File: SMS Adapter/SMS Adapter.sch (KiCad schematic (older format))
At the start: 3 parts, among them J1 c64_idc, J2 sms_joypad, J3 FIRE_SWAP

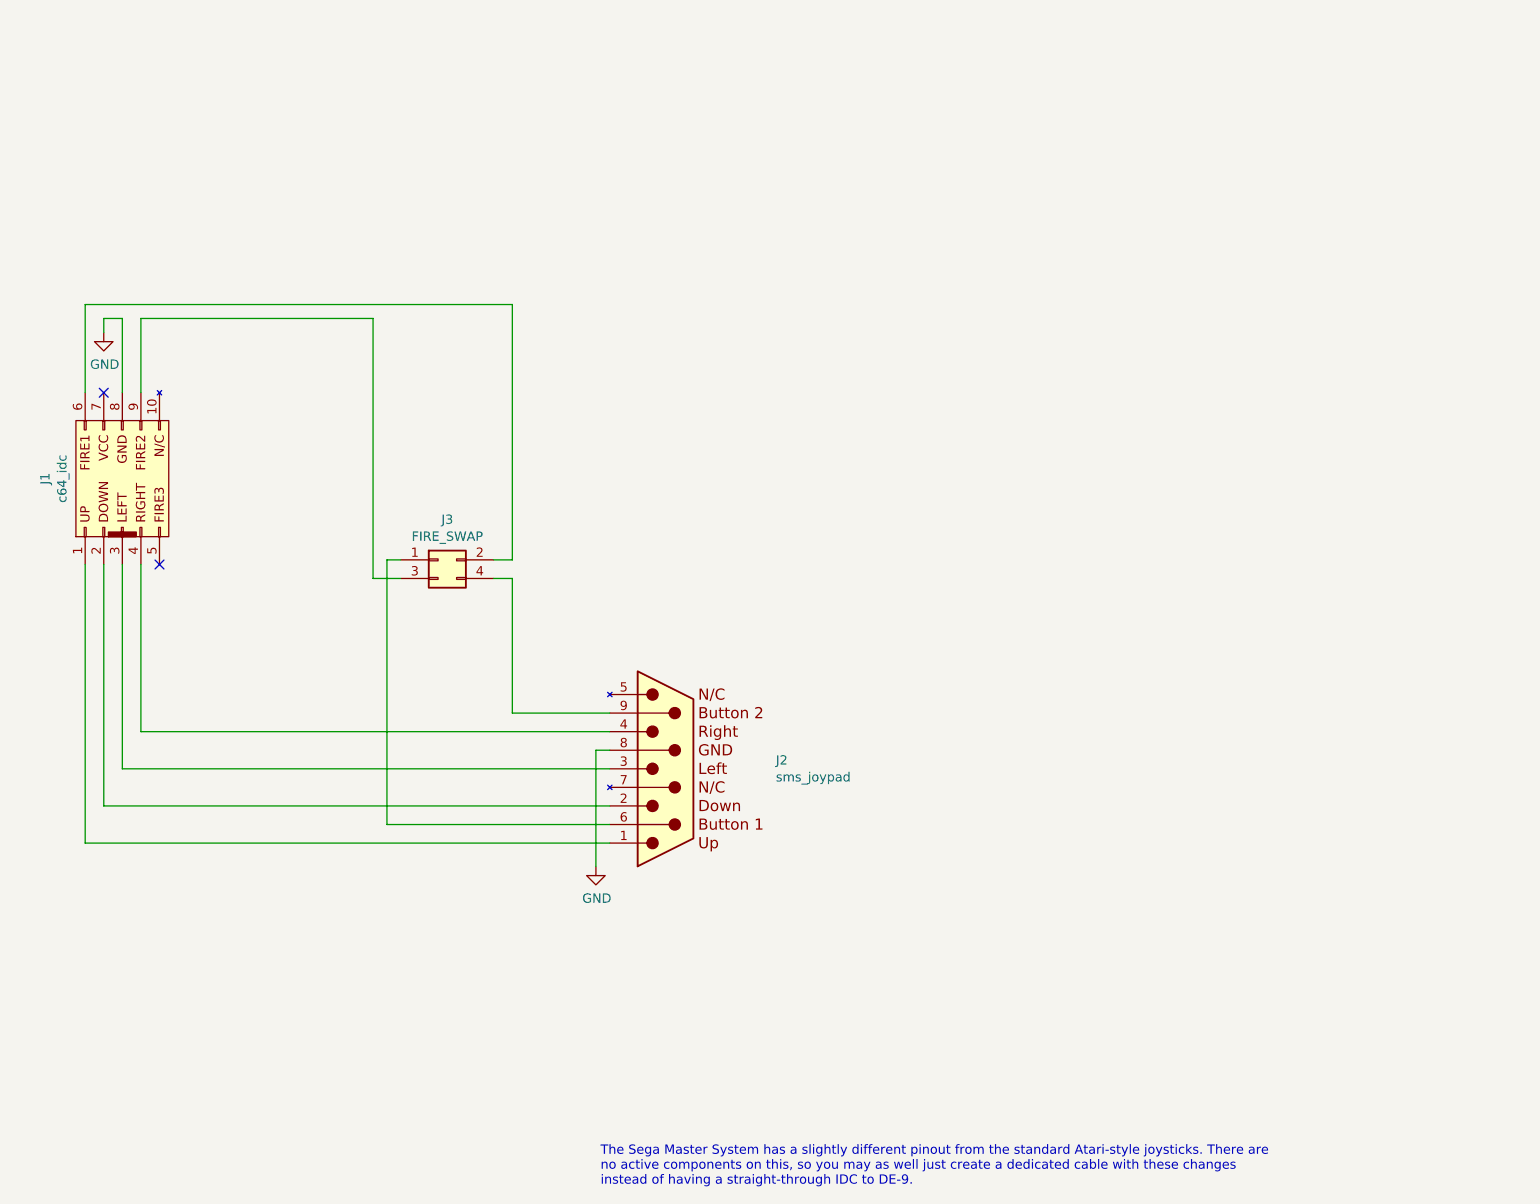
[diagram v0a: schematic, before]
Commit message: Added SMS jumper settings to schematic
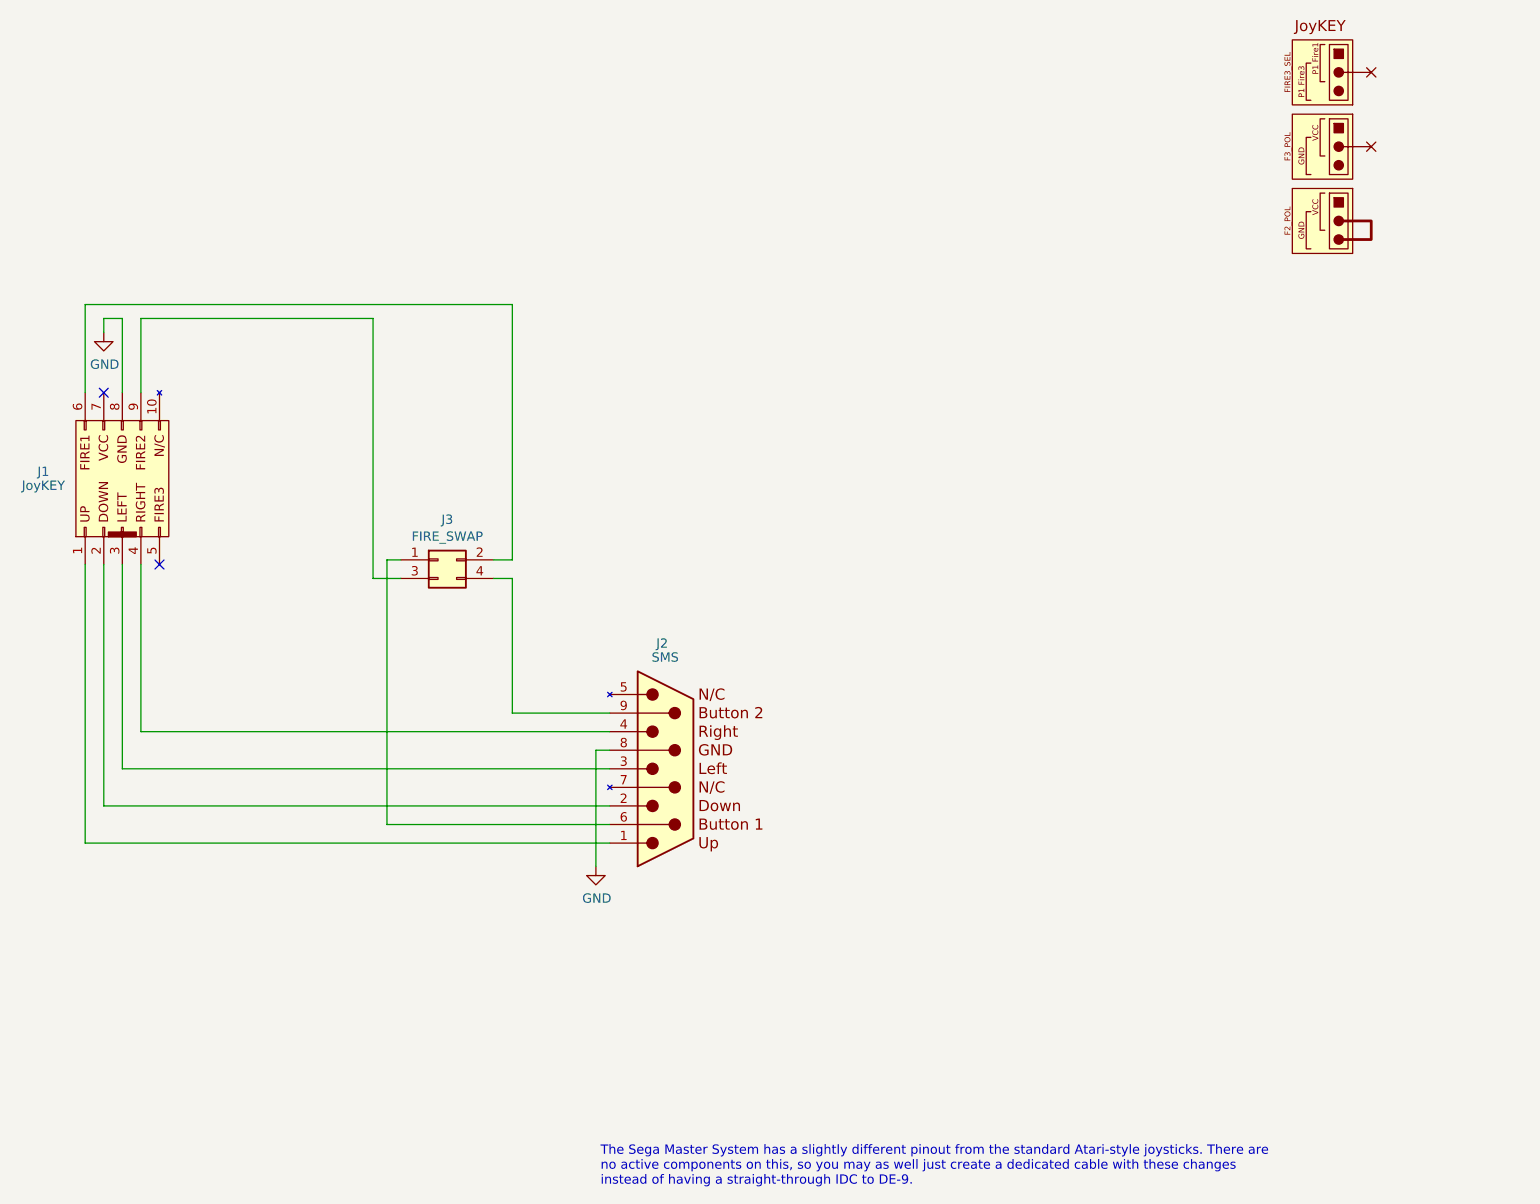
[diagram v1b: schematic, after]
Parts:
- J1: value c64_idc -> JoyKEY
- J2: value sms_joypad -> SMS
- J3: footprint (none) -> Pin_Headers:Pin_Header_Straight_2x02_Pitch2.54mm
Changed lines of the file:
@@
 U 1 1 5FD1F19D
 P 4425 3000
-F 0 "J1" H 4437 3415 50  0000 C CNN
-F 1 "c64_idc" H 4437 3324 50  0000 C CNN
+F 0 "J1" V 4475 3425 50  0000 C CNN
+F 1 "JoyKEY" V 4400 3425 50  0000 C CNN
 F 2 "" H 4425 3000 50  0001 C CNN
 F 3 "~" H 4425 3000 50  0001 C CNN
@@
 U 1 1 5FD232F5
 P 7350 4550
-F 0 "J2" H 7944 4596 50  0000 L CNN
-F 1 "sms_joypad" H 7944 4505 50  0000 L CNN
+F 0 "J2" H 7300 5225 50  0000 L CNN
+F 1 "SMS" H 7275 5150 50  0000 L CNN
 F 2 "" H 7350 4550 50  0001 C CNN
 F 3 "" H 7350 4550 50  0001 C CNN
@@
 F 0 "J3" H 6175 3642 50  0000 C CNN
 F 1 "FIRE_SWAP" H 6175 3551 50  0000 C CNN
-F 2 "" H 6125 3425 50  0001 C CNN
+F 2 "Pin_Headers:Pin_Header_Straight_2x02_Pitch2.54mm" H 6125 3425 50  0001 C CNN
 F 3 "~" H 6125 3425 50  0001 C CNN
 	1    6125 3425
@@
 Text Notes 7000 6800 0    50   ~ 0
 The Sega Master System has a slightly different pinout from the standard Atari-style joysticks. There are\nno active components on this, so you may as well just create a dedicated cable with these changes \ninstead of having a straight-through IDC to DE-9.
+$Comp
+L joykey_jumpers:JUMPER_SETTINGS_1 #1
+U 1 1 5FD24880
+P 10975 700
+F 0 "#1" H 10875 825 50  0001 C CNN
+F 1 "JUMPER_SETTINGS_1" H 10850 -450 50  0001 C CNN
+F 2 "" H 10975 525 50  0001 C CNN
+F 3 "~" H 10975 525 50  0001 C CNN
+	1    10975 700
+	1    0    0    -1
+$EndComp
+$Comp
+L joykey_jumpers:JUMPER_CONNECTED #4
+U 1 1 5FD250F4
+P 10975 1650
+F 0 "#4" H 10975 1550 50  0001 C CNN
+F 1 "JUMPER_CONNECTED" H 10975 1750 50  0001 C CNN
+F 2 "" H 10975 1650 50  0001 C CNN
+F 3 "" H 10975 1650 50  0001 C CNN
+	1    10975 1650
+	1    0    0    -1
+$EndComp
+$Comp
+L joykey_jumpers:JUMPER_NOT_CONNECTED #3
+U 1 1 5FD25605
+P 10975 1200
+F 0 "#3" H 10975 1125 50  0001 C CNN
+F 1 "JUMPER_NOT_CONNECTED" H 10975 1300 50  0001 C CNN
+F 2 "" H 10975 1200 50  0001 C CNN
+F 3 "" H 10975 1200 50  0001 C CNN
+	1    10975 1200
+	1    0    0    -1
+$EndComp
+$Comp
+L joykey_jumpers:JUMPER_NOT_CONNECTED #2
+U 1 1 5FD25BFC
+P 10975 800
+F 0 "#2" H 10975 725 50  0001 C CNN
+F 1 "JUMPER_NOT_CONNECTED" H 10975 900 50  0001 C CNN
+F 2 "" H 10975 800 50  0001 C CNN
+F 3 "" H 10975 800 50  0001 C CNN
+	1    10975 800
+	1    0    0    -1
+$EndComp
 $EndSCHEMATC

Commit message: SMS Adapter PCB
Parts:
- removed J3: FIRE_SWAP, Pin_Headers:Pin_Header_Straight_2x02_Pitch2.54mm, symbol Connector_Generic:Conn_02x02_Odd_Even
- added JP1: FIRE1_SEL, Pin_Headers:Pin_Header_Straight_1x03_Pitch2.54mm, symbol Jumper:Jumper_3_Bridged12
- added JP2: FIRE2_SEL, Pin_Headers:Pin_Header_Straight_1x03_Pitch2.54mm, symbol Jumper:Jumper_3_Bridged12
- J1: footprint (none) -> C64 IDC:IDC_Joystick
- J2: footprint (none) -> RND_DSUB:DSUB-9_Female_Edge
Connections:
- net UP: now reaches J1.1 (Pin_1), J2.1
- net DOWN: now reaches J1.2 (Pin_2), J2.2
- net LEFT: now reaches J1.3 (Pin_3), J2.3
- net RIGHT: now reaches J1.4 (Pin_4), J2.4
- net FIRE1_IN: now reaches J1.6 (Pin_6)
- net FIRE1_IN: now also JP1.1 (A), JP2.3 (B)
- net FIRE2_IN: now reaches J1.9 (Pin_9)
- net FIRE2_IN: now also JP1.3 (B), JP2.1 (A)
- net FIRE1: now reaches J2.6
- net FIRE1: now also JP1.2 (C)
- net FIRE2: now reaches J2.9
- net FIRE2: now also JP2.2 (C)
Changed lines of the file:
@@
 F 0 "J1" V 4475 3425 50  0000 C CNN
 F 1 "JoyKEY" V 4400 3425 50  0000 C CNN
-F 2 "" H 4425 3000 50  0001 C CNN
+F 2 "C64 IDC:IDC_Joystick" H 4425 3000 50  0001 C CNN
 F 3 "~" H 4425 3000 50  0001 C CNN
 	1    4425 3000
@@
 F 0 "J2" H 7300 5225 50  0000 L CNN
 F 1 "SMS" H 7275 5150 50  0000 L CNN
-F 2 "" H 7350 4550 50  0001 C CNN
+F 2 "RND_DSUB:DSUB-9_Female_Edge" H 7350 4550 50  0001 C CNN
 F 3 "" H 7350 4550 50  0001 C CNN
 	1    7350 4550
 	1    0    0    -1
 $EndComp
-$Comp
-L Connector_Generic:Conn_02x02_Odd_Even J3
-U 1 1 5FD268A5
-P 6125 3425
-F 0 "J3" H 6175 3642 50  0000 C CNN
-F 1 "FIRE_SWAP" H 6175 3551 50  0000 C CNN
-F 2 "Pin_Headers:Pin_Header_Straight_2x02_Pitch2.54mm" H 6125 3425 50  0001 C CNN
-F 3 "~" H 6125 3425 50  0001 C CNN
-	1    6125 3425
-	1    0    0    -1
-$EndComp
 NoConn ~ 4625 3450
 Wire Wire Line
-	6525 3425 6425 3425
-Wire Wire Line
-	5775 3525 5925 3525
-Wire Wire Line
-	5925 3425 5850 3425
-Wire Wire Line
-	5850 3425 5850 4850
-Wire Wire Line
 	5850 4850 7050 4850
-Wire Wire Line
-	6425 3525 6525 3525
-Wire Wire Line
-	6525 3525 6525 4250
-Wire Wire Line
-	6525 4250 7050 4250
 Wire Wire Line
 	7050 4450 6975 4450
@@
 	4425 2125 4425 2525
 Wire Wire Line
-	4525 2125 5775 2125
-Wire Wire Line
 	4525 2125 4525 2525
 Wire Wire Line
-	5775 2125 5775 3525
-Wire Wire Line
-	4225 2050 6525 2050
-Wire Wire Line
 	4225 2050 4225 2525
-Wire Wire Line
-	6525 2050 6525 3425
 Text Notes 7000 6800 0    50   ~ 0
 The Sega Master System has a slightly different pinout from the standard Atari-style joysticks. There are\nno active components on this, so you may as well just create a dedicated cable with these changes \ninstead of having a straight-through IDC to DE-9.
@@
 	1    0    0    -1
 $EndComp
+Text Label 4450 4550 0    50   ~ 0
+LEFT
+Text Label 4550 4350 0    50   ~ 0
+RIGHT
+Text Label 4250 4950 0    50   ~ 0
+UP
+Text Label 4350 4750 0    50   ~ 0
+DOWN
+Text Label 5875 4850 0    50   ~ 0
+FIRE1
+Text Label 5975 4250 0    50   ~ 0
+FIRE2
+$Comp
+L Jumper:Jumper_3_Bridged12 JP1
+U 1 1 5FD2FDB9
+P 5600 2450
+F 0 "JP1" V 5554 2517 50  0000 L CNN
+F 1 "FIRE1_SEL" V 5645 2517 50  0000 L CNN
+F 2 "Pin_Headers:Pin_Header_Straight_1x03_Pitch2.54mm" H 5600 2450 50  0001 C CNN
+F 3 "~" H 5600 2450 50  0001 C CNN
+	1    5600 2450
+	0    -1   1    0
+$EndComp
+$Comp
+L Jumper:Jumper_3_Bridged12 JP2
+U 1 1 5FD30CB5
+P 5600 3325
+F 0 "JP2" V 5646 3392 50  0000 L CNN
+F 1 "FIRE2_SEL" V 5555 3392 50  0000 L CNN
+F 2 "Pin_Headers:Pin_Header_Straight_1x03_Pitch2.54mm" H 5600 3325 50  0001 C CNN
+F 3 "~" H 5600 3325 50  0001 C CNN
+	1    5600 3325
+	0    -1   -1   0
+$EndComp
+Wire Wire Line
+	5600 2050 5600 2200
+Wire Wire Line
+	5600 2800 5600 2700
+Wire Wire Line
+	5600 3575 5600 3625
+Wire Wire Line
+	4950 3625 4950 2800
+Wire Wire Line
+	4950 3625 5600 3625
+Wire Wire Line
+	4950 2800 5600 2800
+Connection ~ 4950 2800
+Wire Wire Line
+	4950 2800 4950 2125
+Wire Wire Line
+	5600 3075 5600 3000
+Wire Wire Line
+	5600 3000 5050 3000
+Wire Wire Line
+	5050 3000 5050 2050
+Connection ~ 5050 2050
+Wire Wire Line
+	5050 2050 5600 2050
+Wire Wire Line
+	5850 2450 5850 4850
+Wire Wire Line
+	5950 3325 5950 4250
+Wire Wire Line
+	5950 4250 7050 4250
+Text Label 4250 2050 0    50   ~ 0
+FIRE1_IN
+Text Label 4550 2125 0    50   ~ 0
+FIRE2_IN
+Wire Wire Line
+	5750 2450 5850 2450
+Wire Wire Line
+	5750 3325 5950 3325
+Wire Wire Line
+	4225 2050 5050 2050
+Wire Wire Line
+	4525 2125 4950 2125
 $EndSCHEMATC
